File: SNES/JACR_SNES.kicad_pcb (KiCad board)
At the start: 2 copper layers, 90.1 x 53.3 mm, 9 parts, among them J1 JACR CARTRIDGE ADAPTER, J2 SNES Cartridge Slot

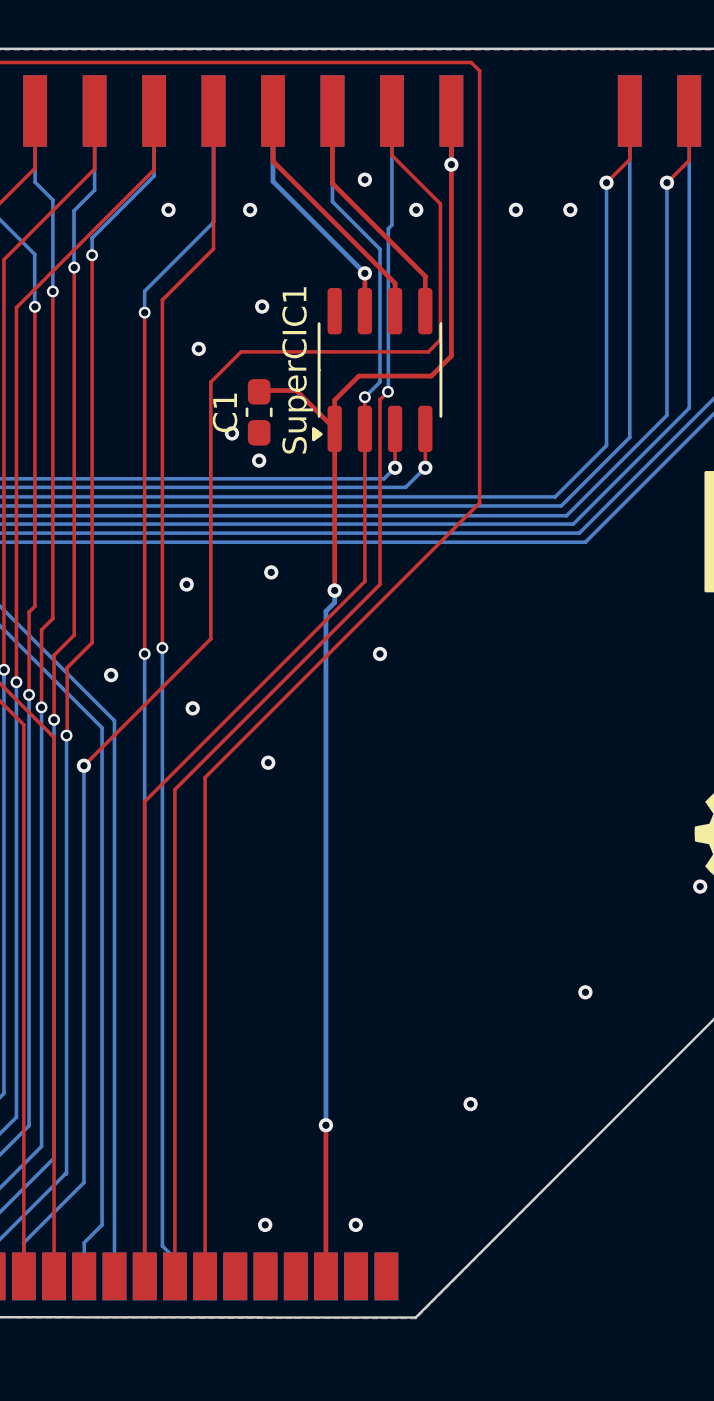
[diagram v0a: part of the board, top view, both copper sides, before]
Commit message: JACR connector was modified, voltage pins were changed
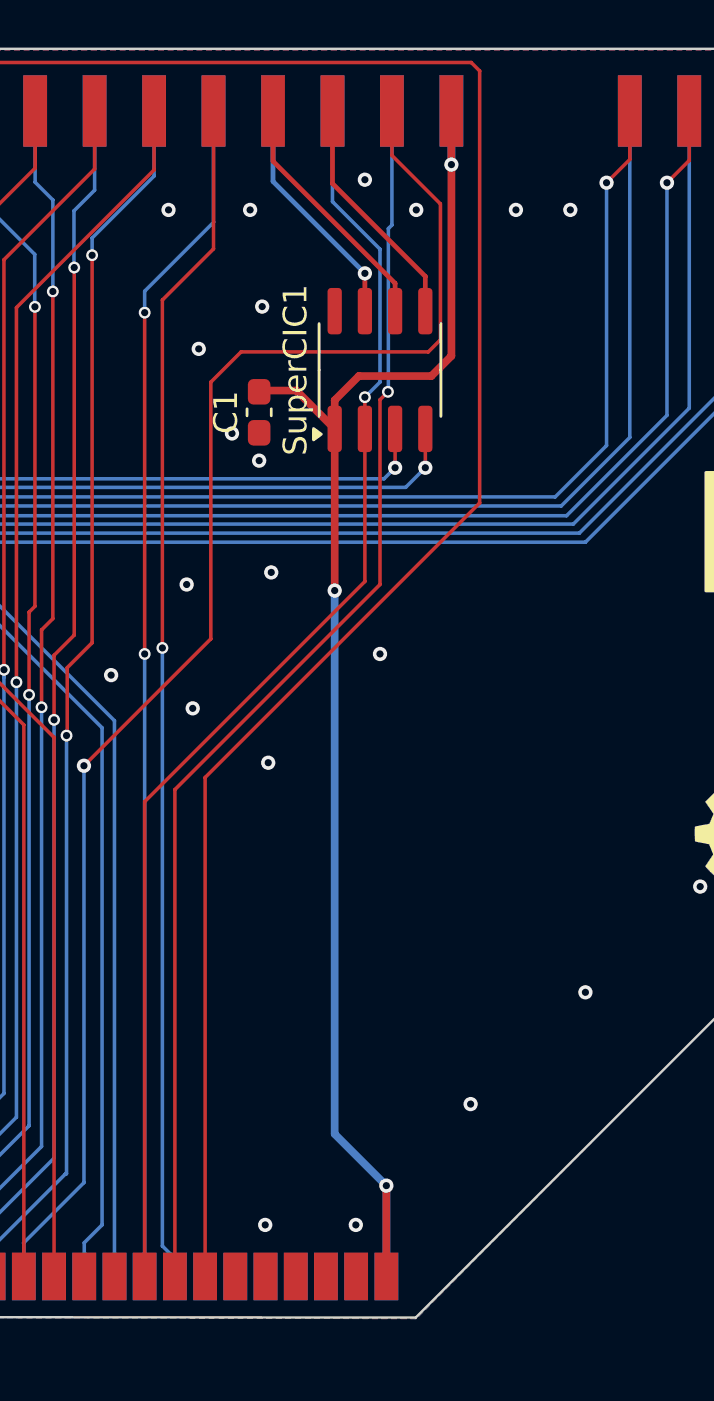
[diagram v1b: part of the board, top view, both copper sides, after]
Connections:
- J1 pad 75: +5V -> unconnected-(J1-+3V3-Pad75)
- J1 pad 79: unconnected-(J1-+12V-Pad79) -> +5V
- J1 pad 80: unconnected-(J1-+12V-Pad80) -> +5V
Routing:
- net +5V: track 59.4 -> 63.5 mm
